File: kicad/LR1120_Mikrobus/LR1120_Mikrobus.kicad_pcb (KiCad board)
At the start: 4 copper layers, 57.2 x 25.4 mm, 109 parts, among them CON1 MIKROBUS_MODULE_CONN, J1 Conn_01x07, J2 Conn_01x07, Q1 NX2016SA-32M-EXS00A-CS06465, Q2 NT2016SA-32M-END4263A, Q3 NX3215SA, U1 LR1120, U2 SKY13588-460LF, U5 LIS2DE12, U7 M24128-BFMH6TG, U8 BGA524N6E6327XTSA1

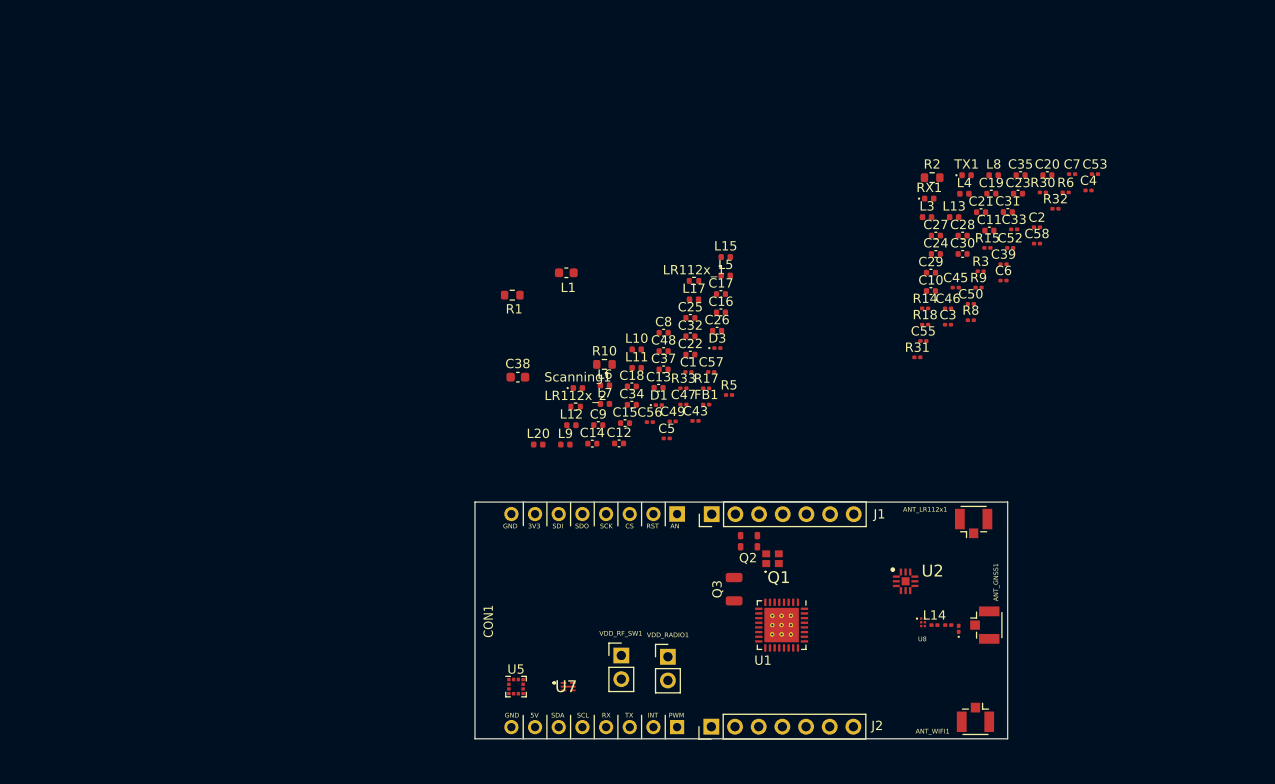
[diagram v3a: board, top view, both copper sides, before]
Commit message: more components placed
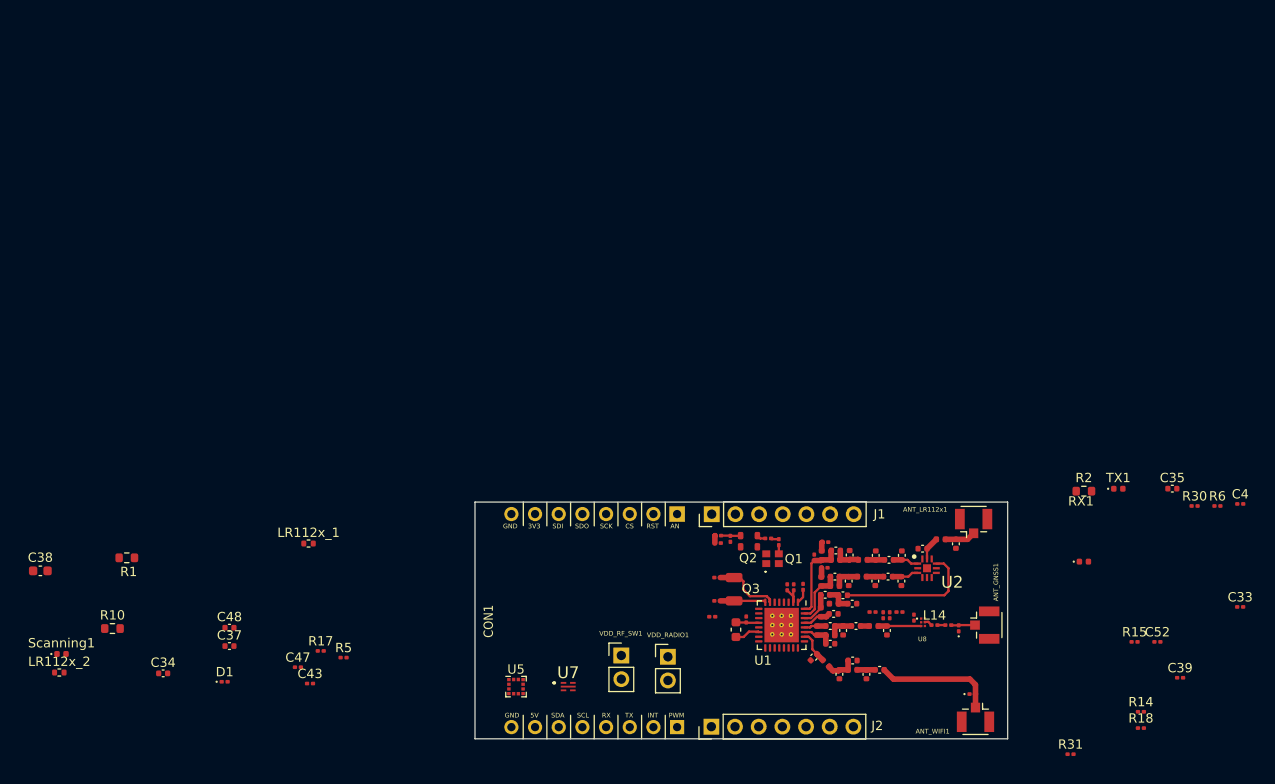
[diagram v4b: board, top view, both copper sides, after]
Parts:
- C53: footprint Capacitor_SMD:C_0201_0603Metric -> Capacitor_SMD:C_0402_1005Metric
- moved LR112x_2 62.3 mm to (55.4, 118.3)
- moved Scanning1 62.3 mm to (55.6, 116.3)
- moved R10 59.9 mm to (61.1, 113.6)
- moved C53 58.3 mm to (140.5, 117.0)
- moved C34 58.0 mm to (66.5, 118.4)
- moved R32 57.2 mm to (125.5, 112.3)
- moved C38 55.3 mm to (53.4, 107.4)
- moved C37 55.2 mm to (73.7, 115.5)
- moved C48 55.2 mm to (73.7, 113.5)
- moved D1 55.2 mm to (73.1, 119.3)
- moved C23 50.6 mm to (138.1, 113.3)
- moved C20 50.5 mm to (140.5, 110.9), turned to 180 degrees
- moved LR112x_1 50.0 mm to (82.1, 104.5)
- moved R1 50.0 mm to (62.6, 106.0)
- moved C43 50.0 mm to (82.3, 119.5)
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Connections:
- C50 pad 1: /XTA -> Net-(C50-Pad1)
- Q2 pad 1: GND -> Net-(C49-Pad1)
- Q2 pad 2: GND -> Net-(C50-Pad2)
- Q2 pad 3: Net-(C50-Pad2) -> GND
- Q2 pad 4: Net-(C49-Pad1) -> GND
- R3 pad 1: GND -> /XTA
- R3 pad 2: /XTA -> Net-(C50-Pad1)
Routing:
- net Net-(C21-Pad2): track 0.00 -> 15.0 mm
- net Net-(ANT_WIFI1-Pad1): track 0.00 -> 12.9 mm
- net Net-(C8-Pad1): track 0.00 -> 8.78 mm
- net /DIO11: track 0.00 -> 7.13 mm
- net /RFO_LP_LF: track 0.00 -> 6.06 mm
- net /DIO10: track 0.00 -> 4.89 mm
- net Net-(C26-Pad2): track 0.00 -> 4.60 mm
- net Net-(C19-Pad1): track 0.00 -> 3.64 mm
- net Net-(C27-Pad1): track 0.00 -> 3.58 mm
- net /VR_PA: track 0.00 -> 3.51 mm
- net Net-(C22-Pad2): track 0.00 -> 3.33 mm
- net Net-(ANT_LR112x1-Pad1): track 0.00 -> 3.30 mm
- net Net-(C28-Pad1): track 0.00 -> 3.30 mm
- net Net-(C18-Pad2): track 0.00 -> 3.04 mm
- net Net-(C8-Pad2): track 0.00 -> 3.01 mm
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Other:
- rule pad_to_mask_clearance: 0 -> 0.001
